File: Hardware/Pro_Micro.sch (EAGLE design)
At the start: 33 parts, among them U2 MIC5219, U3 ATMEGA32U4, X1 USB-MICROB, Y1 16MHz

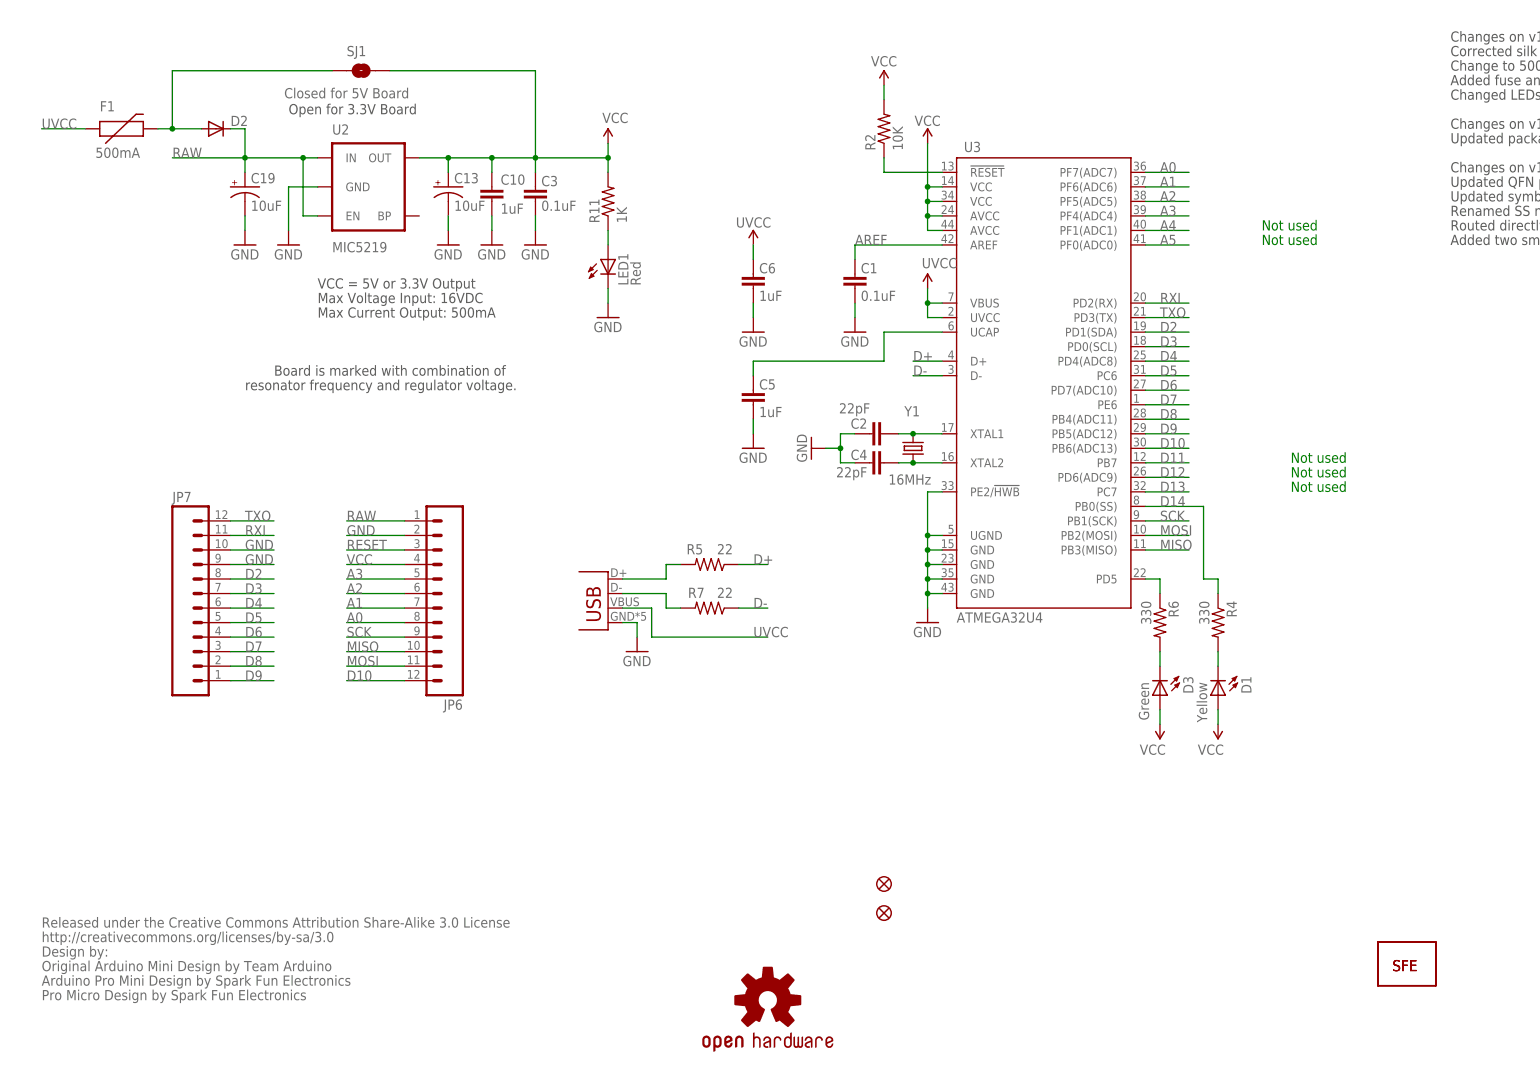
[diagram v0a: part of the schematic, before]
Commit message: Updated v13 design files
Updated usb connector, IC footprint and route job and moved from 0402 to
0603.
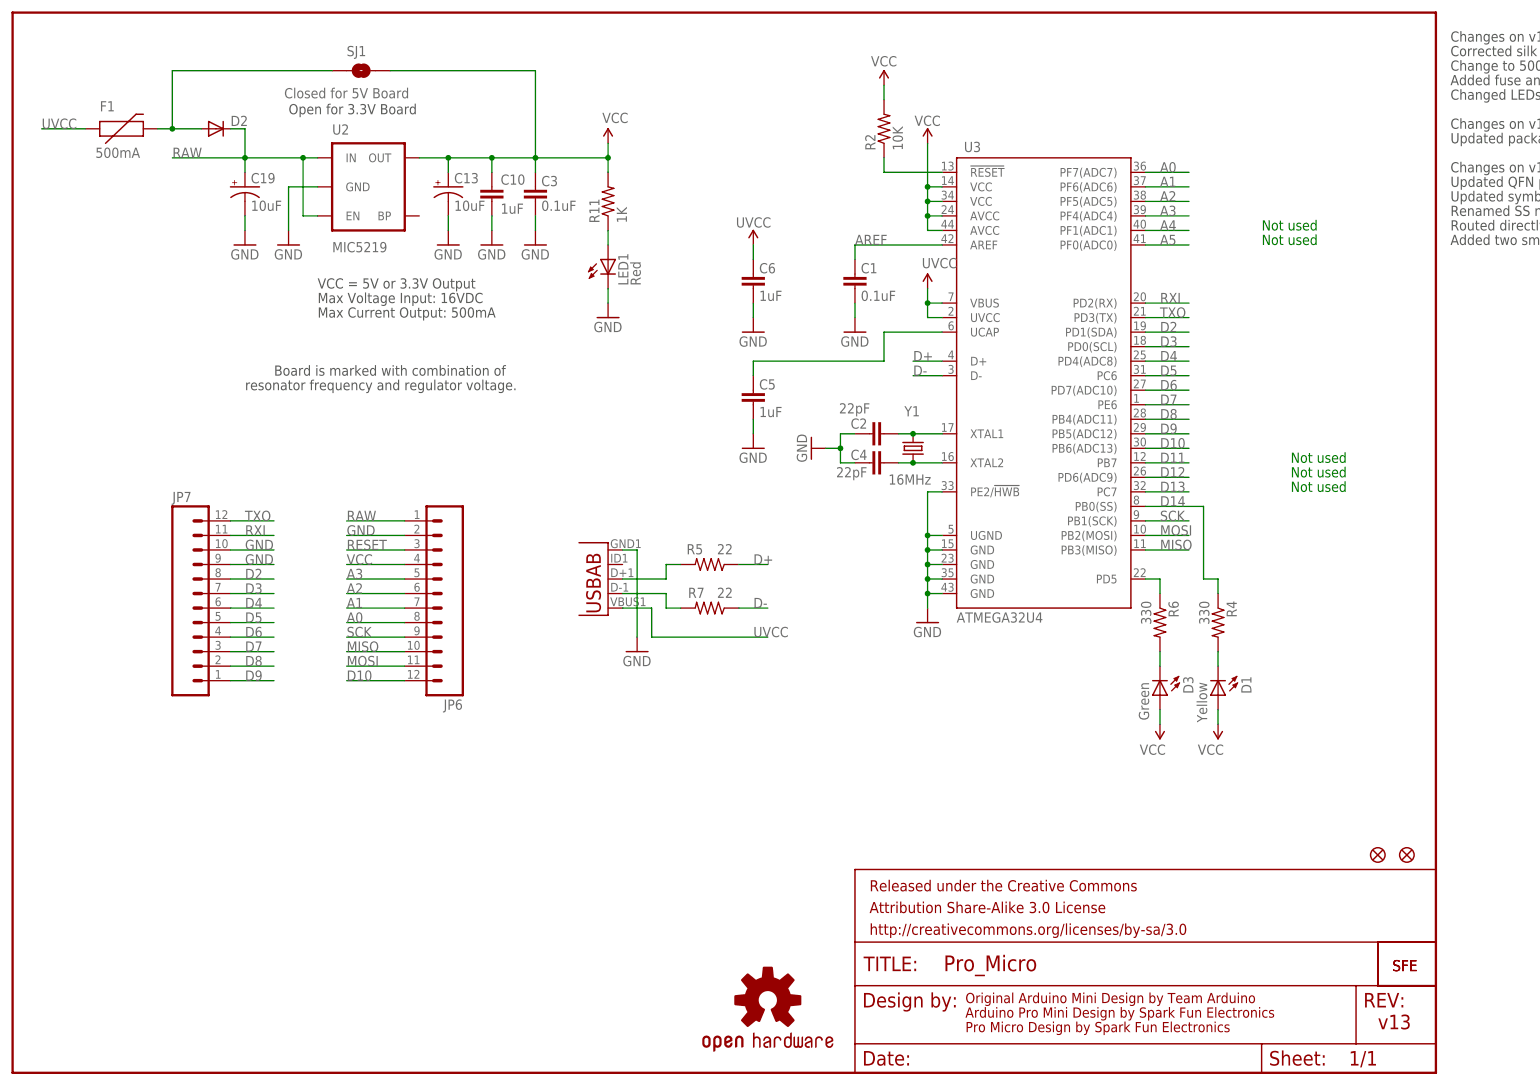
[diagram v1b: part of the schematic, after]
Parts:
- removed U$5: CREATIVE_COMMONS, SparkFun:CREATIVE_COMMONS
- added FRAME1: FRAME-LETTER, SparkFun-Aesthetics:FRAME-LETTER
- U3: device Testing:ATMEGA32U41:1 -> Testing:ATMEGA32U4OUTFAKES
- X1: value USB-MICROB -> (none); device SparkFun-Connectors:USB-MICROB -> Testing:USB-ABIN&OUT
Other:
- note added: "v13"
